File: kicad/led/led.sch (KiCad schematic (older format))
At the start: 3 parts

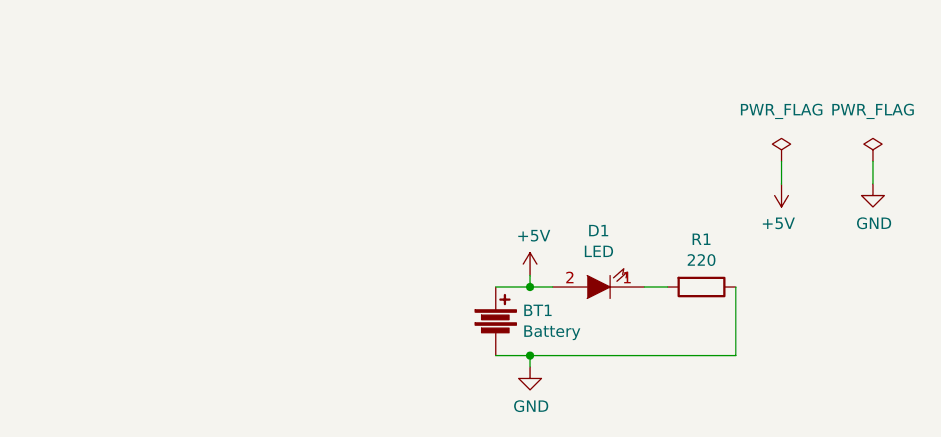
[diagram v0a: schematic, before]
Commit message: make it compatible with kicad recent version
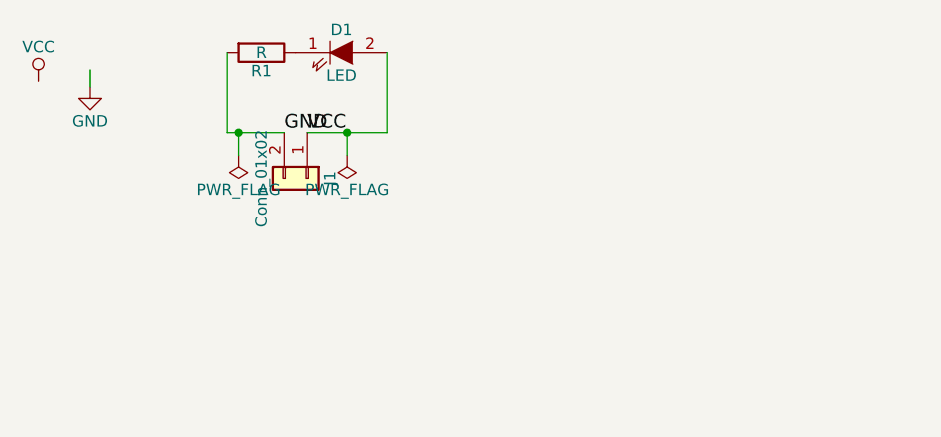
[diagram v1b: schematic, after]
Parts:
- removed BT1: Battery, Battery_Holders:Keystone_103_1x20mm-CoinCell, symbol Battery
- added J1: Conn_01x02, Pin_Headers:Pin_Header_Straight_1x02_Pitch2.00mm, symbol Conn_01x02
- D1: footprint LEDs:LED-3MM -> LEDs:LED_0603_HandSoldering
- R1: value 220 -> R
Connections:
- net labels added: VCC
- net labels removed: +5V
- wire segments 8 -> 7
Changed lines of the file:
@@
 EESchema Schematic File Version 2
 LIBS:power
+LIBS:MyLibrary
 LIBS:device
 LIBS:transistors
@@
 $Comp
 L LED D1
-U 1 1 580C3B94
-P 6500 3600
-F 0 "D1" H 6500 3355 50  0000 C CNN
-F 1 "LED" H 6500 3446 50  0000 C CNN
-F 2 "LEDs:LED-3MM" H 6500 3600 50  0001 C CNN
-F 3 "" H 6500 3600 50  0000 C CNN
-	1    6500 3600
-	-1   0    0    1
-$EndComp
-$Comp
-L PWR_FLAG #FLG01
-U 1 1 580C3CA0
-P 7300 3050
-F 0 "#FLG01" H 7300 3145 50  0001 C CNN
-F 1 "PWR_FLAG" H 7300 3274 50  0000 C CNN
-F 2 "" H 7300 3050 50  0000 C CNN
-F 3 "" H 7300 3050 50  0000 C CNN
-	1    7300 3050
-	1    0    0    -1
-$EndComp
-$Comp
-L +5V #PWR02
-U 1 1 580C3CB6
-P 6200 3550
-F 0 "#PWR02" H 6200 3400 50  0001 C CNN
-F 1 "+5V" H 6215 3723 50  0000 C CNN
-F 2 "" H 6200 3550 50  0000 C CNN
-F 3 "" H 6200 3550 50  0000 C CNN
-	1    6200 3550
+U 1 1 59FF13BA
+P 5375 2575
+F 0 "D1" H 5375 2675 50  0000 C CNN
+F 1 "LED" H 5375 2475 50  0000 C CNN
+F 2 "LEDs:LED_0603_HandSoldering" H 5375 2575 50  0001 C CNN
+F 3 "" H 5375 2575 50  0000 C CNN
+	1    5375 2575
 	1    0    0    -1
 $EndComp
 $Comp
 L R R1
-U 1 1 580C3CCC
-P 6950 3600
-F 0 "R1" V 6743 3600 50  0000 C CNN
-F 1 "220" V 6834 3600 50  0000 C CNN
-F 2 "Resistors_SMD:R_0603_HandSoldering" V 6880 3600 50  0001 C CNN
-F 3 "" H 6950 3600 50  0000 C CNN
-	1    6950 3600
+U 1 1 59FF1465
+P 5025 2575
+F 0 "R1" V 5105 2575 50  0000 C CNN
+F 1 "R" V 5025 2575 50  0000 C CNN
+F 2 "Resistors_SMD:R_0603_HandSoldering" V 4955 2575 50  0001 C CNN
+F 3 "" H 5025 2575 50  0000 C CNN
+	1    5025 2575
 	0    1    1    0
 $EndComp
 $Comp
-L GND #PWR03
-U 1 1 580C3D0F
-P 6200 3950
-F 0 "#PWR03" H 6200 3700 50  0001 C CNN
-F 1 "GND" H 6205 3777 50  0000 C CNN
-F 2 "" H 6200 3950 50  0000 C CNN
-F 3 "" H 6200 3950 50  0000 C CNN
-	1    6200 3950
+L Conn_01x02 J1
+U 1 1 59FF1494
+P 5225 3125
+F 0 "J1" H 5225 3225 50  0000 C CNN
+F 1 "Conn_01x02" H 5225 2925 50  0000 C CNN
+F 2 "Pin_Headers:Pin_Header_Straight_1x02_Pitch2.00mm" H 5225 3125 50  0001 C CNN
+F 3 "" H 5225 3125 50  0001 C CNN
+	1    5225 3125
+	0    1    1    0
+$EndComp
+Wire Wire Line
+	4875 2925 5125 2925
+Wire Wire Line
+	4875 2575 4875 2925
+Wire Wire Line
+	5575 2575 5575 2925
+Wire Wire Line
+	5575 2925 5225 2925
+$Comp
+L PWR_FLAG #FLG01
+U 1 1 59FF15E9
+P 5400 3025
+F 0 "#FLG01" H 5400 3100 50  0001 C CNN
+F 1 "PWR_FLAG" H 5400 3175 50  0000 C CNN
+F 2 "" H 5400 3025 50  0001 C CNN
+F 3 "" H 5400 3025 50  0001 C CNN
+	1    5400 3025
+	-1   0    0    1
+$EndComp
+Wire Wire Line
+	5400 3025 5400 2925
+Connection ~ 5400 2925
+$Comp
+L PWR_FLAG #FLG02
+U 1 1 59FF161F
+P 4925 3025
+F 0 "#FLG02" H 4925 3100 50  0001 C CNN
+F 1 "PWR_FLAG" H 4925 3175 50  0000 C CNN
+F 2 "" H 4925 3025 50  0001 C CNN
+F 3 "" H 4925 3025 50  0001 C CNN
+	1    4925 3025
+	-1   0    0    1
+$EndComp
+Wire Wire Line
+	4925 3025 4925 2925
+Connection ~ 4925 2925
+$Comp
+L VCC #PWR03
+U 1 1 59FF1754
+P 4050 2700
+F 0 "#PWR03" H 4050 2550 50  0001 C CNN
+F 1 "VCC" H 4050 2850 50  0000 C CNN
+F 2 "" H 4050 2700 50  0001 C CNN
+F 3 "" H 4050 2700 50  0001 C CNN
+	1    4050 2700
 	1    0    0    -1
 $EndComp
 $Comp
-L +5V #PWR04
-U 1 1 580C3D71
-P 7300 3150
-F 0 "#PWR04" H 7300 3000 50  0001 C CNN
-F 1 "+5V" H 7315 3323 50  0000 C CNN
-F 2 "" H 7300 3150 50  0000 C CNN
-F 3 "" H 7300 3150 50  0000 C CNN
-	1    7300 3150
-	-1   0    0    1
-$EndComp
-$Comp
-L PWR_FLAG #FLG05
-U 1 1 580C3DAD
-P 7700 3050
-F 0 "#FLG05" H 7700 3145 50  0001 C CNN
-F 1 "PWR_FLAG" H 7700 3274 50  0000 C CNN
-F 2 "" H 7700 3050 50  0000 C CNN
-F 3 "" H 7700 3050 50  0000 C CNN
-	1    7700 3050
-	1    0    0    -1
-$EndComp
-$Comp
-L GND #PWR06
-U 1 1 580C3DC5
-P 7700 3150
-F 0 "#PWR06" H 7700 2900 50  0001 C CNN
-F 1 "GND" H 7705 2977 50  0000 C CNN
-F 2 "" H 7700 3150 50  0000 C CNN
-F 3 "" H 7700 3150 50  0000 C CNN
-	1    7700 3150
+L GND #PWR04
+U 1 1 59FF176E
+P 4275 2725
+F 0 "#PWR04" H 4275 2475 50  0001 C CNN
+F 1 "GND" H 4275 2575 50  0000 C CNN
+F 2 "" H 4275 2725 50  0001 C CNN
+F 3 "" H 4275 2725 50  0001 C CNN
+	1    4275 2725
 	1    0    0    -1
 $EndComp
 Wire Wire Line
-	7700 3050 7700 3150
-$Comp
-L Battery BT1
-U 1 1 580C3E47
-P 6050 3750
-F 0 "BT1" H 6168 3796 50  0000 L CNN
-F 1 "Battery" H 6168 3705 50  0000 L CNN
-F 2 "Battery_Holders:Keystone_103_1x20mm-CoinCell" V 6050 3790 50  0001 C CNN
-F 3 "" V 6050 3790 50  0000 C CNN
-	1    6050 3750
-	1    0    0    -1
-$EndComp
-Wire Wire Line
-	6050 3600 6300 3600
-Wire Wire Line
-	6700 3600 6800 3600
-Wire Wire Line
-	7100 3600 7100 3900
-Wire Wire Line
-	7100 3900 6050 3900
-Wire Wire Line
-	6200 3950 6200 3900
-Connection ~ 6200 3900
-Wire Wire Line
-	6200 3550 6200 3600
-Connection ~ 6200 3600
-Wire Wire Line
-	7300 3050 7300 3150
+	4275 2650 4275 2725
+Text Label 5125 2925 0    60   ~ 0
+GND
+Text Label 5225 2925 0    60   ~ 0
+VCC
 $EndSCHEMATC
